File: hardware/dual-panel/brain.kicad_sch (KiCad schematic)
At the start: 75 parts, among them J1 USB_C_Receptacle_USB2.0_16P, J14 Conn_01x17, J15 Conn_01x17, SW2 BOOTSEL, U1 RP2040, U2 THVD1429, U3 W25Q32JV, U4 SN74AHCT125, U5 AMS1117-5.0, U6 AP7361C-33ER-13, U7 USBLC6-2SC6, U8 LM66200, X1 12MHz ABM8-272-T3

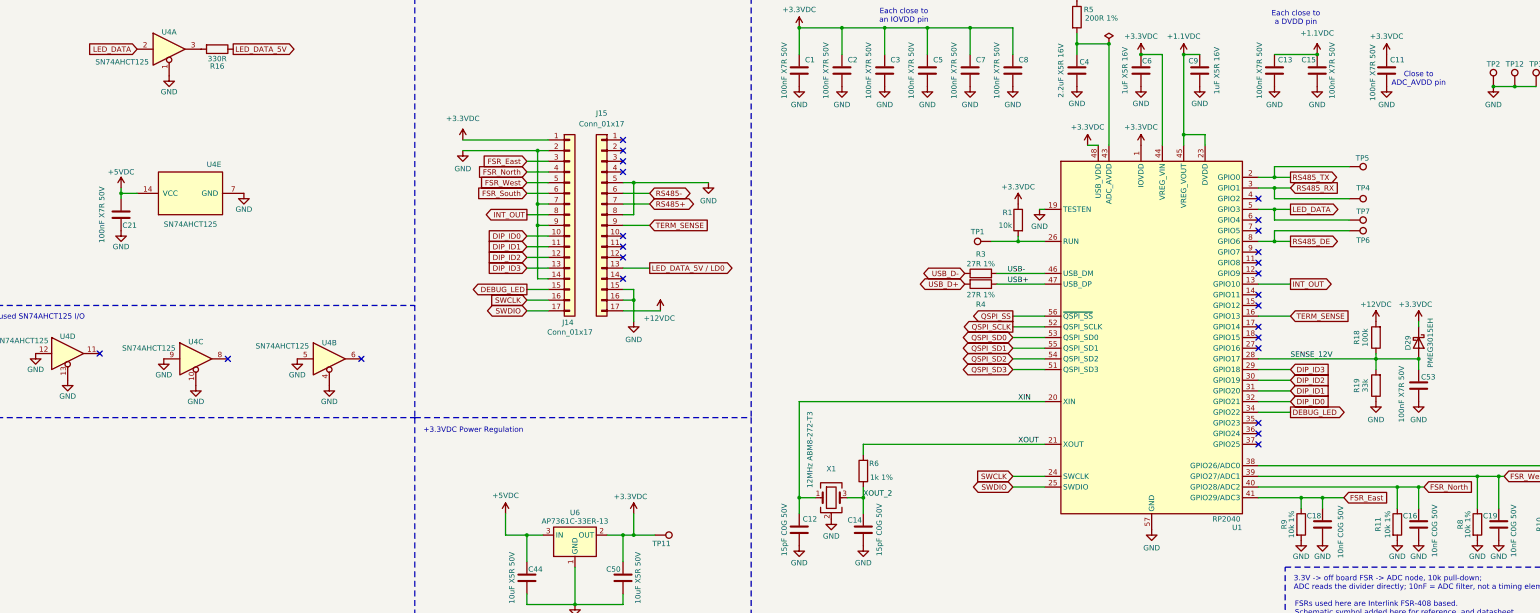
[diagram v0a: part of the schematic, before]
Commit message: dual-panel: brain laid out, interface reworked to 4x 1x8, carrier routed
Work in progress checkpoint — not clean yet, see below.

Interface replaced: the two 1x17 rows became four 1x8 connectors, placed
in the two continuous free bands across the carrier (y~49-58 and y~83-92).
Carrier headers J12/J13/J14/J15 mate with brain sockets J2/J19/J17/J18;
both boards use the same relative layout, since the brain is translated
under the carrier rather than flipped. Grouped by function so the FSR
lines and the fast signals land on separate connectors.

Brain outline drawn at 76.1 x 63.6mm with its own GND_Brain pour, sitting
inside the measured 88 x 100mm frame opening with ~6mm per side in X.
Two M3 holes added per board (carrier H5/H6, brain H1/H2), registered to
the connectors; screw enters from the brain underside with a nut above
the carrier.

Cavity measured: 6mm from the carrier underside to the frame floor, plus
14mm to the cavity bottom, so 20mm of depth inside the opening. That
retires the depth gate and also means the carrier's four remaining
bottom-side parts (D30, R17, R20, C57, tallest 2.3mm) can stay put.

Known open, to fix next:
- +3.3VDC may be split into three islands with the regulator in only one
- +12VDC and VBUS each broken on the brain; VBUS leaves U8 unfed
- FSR_West does not land on R8 pad 1; J1 shell pad floating
- QSPI_SCLK clears GND_Brain by 0 in four places
- 180-degree rotation is only blocked by 0.50mm at the connectors; wants
  a 2.54mm Y delta between J15 and J14 for a half-pitch refusal
- screw scheme needs a board-to-board spacer, and the nuts land inside
  the LED field
- silkscreen deliberately untouched (110 of 115 DRC violations)

ERC 0, schematic parity 0. 25 unconnected, of which roughly 19 are the
expected cross-gap airwires at the mating connectors.
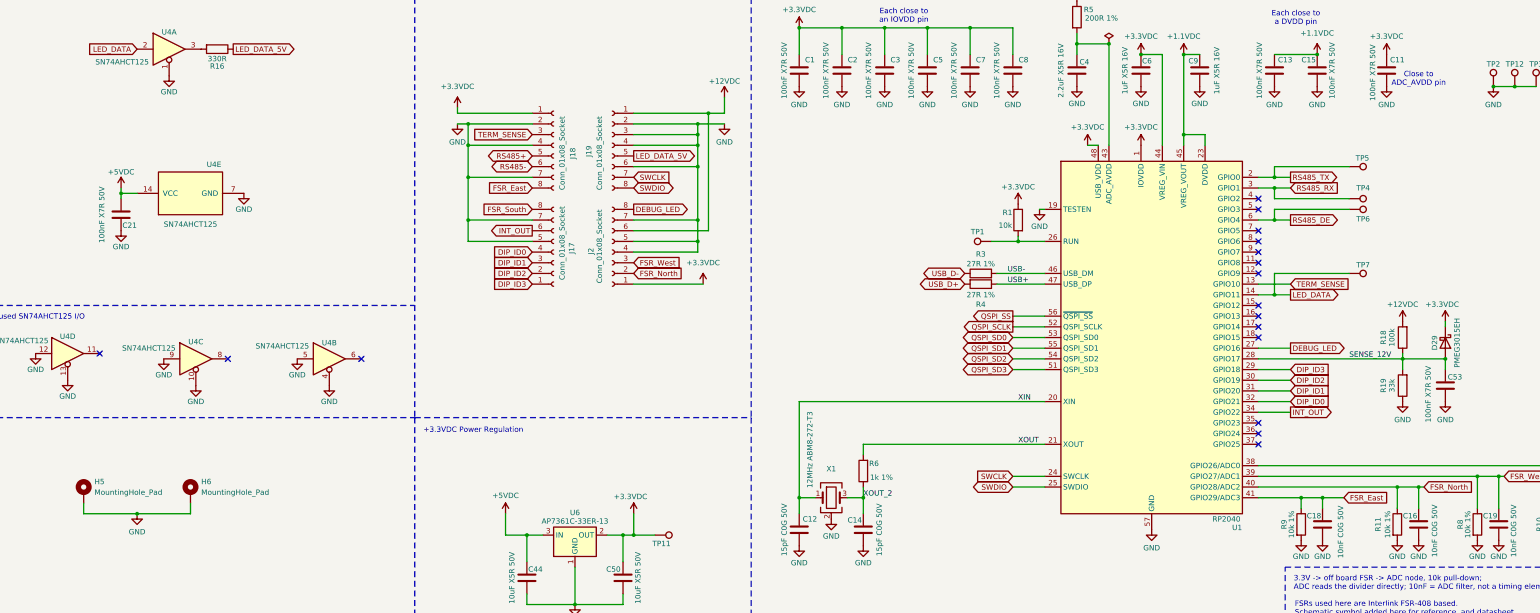
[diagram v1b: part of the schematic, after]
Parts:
- removed J14, J15: Conn_01x17, Connector_PinHeader_2.54mm:PinHeader_1x17_P2.54mm_Vertical, symbol Connector_Generic:Conn_01x17
- added H5, H6: MountingHole_Pad, MountingHole:MountingHole_3.2mm_M3_Pad, symbol Mechanical:MountingHole_Pad
- added J17, J18, J19, J2: Conn_01x08_Socket, Connector_PinSocket_2.54mm:PinSocket_1x08_P2.54mm_Vertical, symbol Connector:Conn_01x08_Socket
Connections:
- net +12VDC: now also J19.1 (Pin_1), J2.6 (Pin_6)
- net +3.3VDC: now also J18.1 (Pin_1), J2.1 (Pin_1)
- net DEBUG_LED: now also U1.27 (GPIO16), J2.8 (Pin_8); no longer U1.34 (GPIO22)
- net DIP_ID0: now also J17.4 (Pin_4)
- net DIP_ID1: now also J17.3 (Pin_3)
- net DIP_ID2: now also J17.2 (Pin_2)
- net DIP_ID3: now also J17.1 (Pin_1)
- net FSR_East: now also J18.8 (Pin_8)
- net FSR_North: now also J2.2 (Pin_2)
- net FSR_South: now also J17.8 (Pin_8)
- net FSR_West: now also J2.3 (Pin_3)
- net GND: now also H5.1, H6.1, J17.5 (Pin_5), J17.7 (Pin_7), J18.2 (Pin_2), J18.4 (Pin_4), J18.7 (Pin_7), J19.2 (Pin_2), J19.3 (Pin_3), J19.4 (Pin_4), J19.6 (Pin_6), J2.4 (Pin_4), J2.5 (Pin_5), J2.7 (Pin_7)
- net INT_OUT: now also U1.34 (GPIO22), J17.6 (Pin_6); no longer U1.13 (GPIO10)
- net LED_DATA: now also U1.14 (GPIO11); no longer U1.5 (GPIO3)
- net LED_DATA_5V: now also J19.5 (Pin_5)
- net RS485+: now also J18.5 (Pin_5)
- net RS485-: now also J18.6 (Pin_6)
- net RS485_DE: now also U1.6 (GPIO4); no longer U1.8 (GPIO6)
- net SWCLK: now also J19.7 (Pin_7)
- net SWDIO: now also J19.8 (Pin_8)
- net TERM_SENSE: now also U1.13 (GPIO10), J18.3 (Pin_3); no longer U1.16 (GPIO13)
- no-connect marks 30 -> 22
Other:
- moved on the sheet: C53, D29, R18, R19, TP6, TP7

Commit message: R8-R11: switch 10k 1% to C98220 for JLC stock
C5713432 was short at JLC, so the FSR divider legs move to C98220. Applied to
both designs, schematic and PCB, since dual-panel and panel-pcb share the part.
C5713432 was used only by these four, so the swap is unambiguous.

These are the FSR voltage-divider legs on the brain, paired with C16-C19. The
mapping is not sequential: N->R11/C16, E->R9/C18, S->R10/C17, W->R8/C19.
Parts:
- R10, R11, R8, R9: LCSC C5713432 -> C98220
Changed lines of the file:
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@@
 			)
 		)
-		(property "LCSC" "C5713432"
+		(property "LCSC" "C98220"
 			(at 386.08 144.78 0)
 			(hide yes)
@@
 			)
 		)
-		(property "LCSC" "C5713432"
+		(property "LCSC" "C98220"
 			(at 347.98 144.78 0)
 			(hide yes)
@@
 			)
 		)
-		(property "LCSC" "C5713432"
+		(property "LCSC" "C98220"
 			(at 325.12 144.78 0)
 			(hide yes)
@@
 			)
 		)
-		(property "LCSC" "C5713432"
+		(property "LCSC" "C98220"
 			(at 367.03 144.78 0)
 			(hide yes)

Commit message: dual-panel: per-sheet refdes blocks, stitching vias, silkscreen
Reference designators are now numbered in per-sheet blocks — carrier 2xx,
brain 3xx — so a designator says which of the two boards a part sits on.
That is the multi-sheet exception the review conventions allow, and it is
cheaper than closing every gap left by seeding both sheets from panel-pcb
and stripping them down. No designator is duplicated across the sheets.

Also: ground stitching vias (464 -> 1071), the year appended to both
name/rev blocks, and the fab order-number placeholder removed.

Note for the next renumber: "Update PCB from Schematic" will refuse to
match and offer to re-add every footprint. The links are fine — it is the
sticky "re-link by reference designator" option, which cannot match once
every designator has changed. Recovery is to revert the annotation,
re-link once while the designators still agree, then reannotate. The
underlying cause is that dual-panel.kicad_pro registers the root sheet as
a1b2c3d4-...-000000000001, which is panel-pcb's root UUID, while
dual-panel.kicad_sch says ...00000000d001.

DRC 0, ERC 0 with zones refilled. 19 unconnected and 93 net_conflict
remain, unchanged from before this commit: the 19 are the board-to-board
mating gap KiCad cannot model, the 93 are pre-existing net-name
disagreements on the WS2815 VCC/PWR_FLAG nets.
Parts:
- renumbered C21 to C301, C52 to C302, C44 to C303, C54 to C304, C56 to C305, C37 to C306, C50 to C307, C38 to C308, C55 to C309, C1 to C310, C12 to C311, C2 to C312, C14 to C313, C3 to C314, C5 to C315, C7 to C316, C8 to C317, C4 to C318, C6 to C319, C9 to C320, C13 to C321, C15 to C322, C20 to C323, C18 to C324, C11 to C325, C16 to C326, C53 to C327, C10 to C328, C19 to C329, C17 to C330, D12 to D301, D23 to D302, D29 to D303, FSR1 to FSR301, H5 to H301, H6 to H302, J18 to J301, J17 to J302, J19 to J303, J2 to J304, J1 to J305, R16 to R301, R6 to R302, R13 to R303, R14 to R304, R3 to R305, R4 to R306, R1 to R307, R5 to R308, R7 to R309, R12 to R310, R9 to R311, R11 to R312, R18 to R313, R19 to R314, R8 to R315, R10 to R316, SW2 to SW301, TP11 to TP301, TP10 to TP302, TP1 to TP303, TP5 to TP304, TP4 to TP305, TP6 to TP306, TP7 to TP307, TP2 to TP308, TP12 to TP309, TP3 to TP310, TP13 to TP311, TP14 to TP312, U4 to U301, U6 to U302, U5 to U303, U8 to U304, U7 to U305, U1 to U306, U3 to U307, U2 to U308, X1 to X301

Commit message: shifter: swap quad SN74AHCT125 for single-gate SN74AHCT1G125 on all boards
External review suggested 74LVC1G34/74LVC1G17 since only one gate was used;
LVC was rejected on input thresholds (VIH = 0.7*VCC = 3.5V at 5V; the 1G17's
Schmitt VT+ max hits 3.33V at 5.5V) but the single-gate idea was right.
SN74AHCT1G125DBVR keeps AHCT's guaranteed TTL VIH of 2.0V in a SOT-23-5:
LCSC C7484, DigiKey 296-4708-1-ND. OE tied to GND; decoupling caps kept.

- panel-pcb U4, dual-panel brain U301, master-pcb U3: schematic symbol,
  footprint, placement and routing redone; spare-gate GND ties and
  no-connects removed
- panel: +5V feed re-routed with a short B.Cu hop under the LED_DATA riser
- master: DIP-14 replaced by SMD; new via drops the B.Cu underglow trace
  onto the A pad, new GND via feeds the OE pad's thermal spokes
- docs + BOMs updated (CLAUDE.md, PANEL_PCB, MASTER_PCB, BOM, UNDERGLOW,
  PRE_ORDER_CHECKLIST, dual-panel README, master-pcb-BOM.csv)

Verification: ERC 0 on all three projects; DRC 0 on panel and master;
dual-panel at its expected floor (19 cross-gap airwires, 90 pre-existing
PWR_FLAG parity conflicts, down from 92).
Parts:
- removed U301: SN74AHCT125, Package_SO:SOIC-14_3.9x8.7mm_P1.27mm, symbol 74xx:74AHCT125
- added U301: SN74AHCT1G125, Package_TO_SOT_SMD:SOT-23-5, symbol 74xGxx:74AHCT1G125
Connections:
- net +5VDC: now also U301.5 (VCC)
- net GND: now also U301.1, U301.3 (GND)
- net LED_DATA: now also U301.2
- net at R301.2: now also U301.4
- no-connect marks 22 -> 19
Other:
- note removed: "Unused SN74AHCT125 I/O"
- moved on the sheet: C301, R301, TP309, TP310

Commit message: dual-panel: third mounting hole, fix hole refdes, set via fill/cap
Adds a third M3 fixing to both boards and moves the top one, which removes
the rocking degree of freedom the two-screw mount still had. With only two
screws the boards could rotate about the axis through them, and the two
board-to-board sockets furthest off that axis sat 27mm and 34mm out. Three
non-collinear fixings constrain the plane outright.

  arrangement                 worst socket-to-screw   support triangle
  2 screws (before)                   45.99 mm        none (collinear)
  old top + new bottom-right          41.46 mm        1576 mm2
  top moved + new bottom-right        32.07 mm        1583 mm2

Brain/carrier hole pairs stay on the exact (101.68, -16.87) offset.

Mounting hole refdes were swapped against the 2xx=carrier / 3xx=brain
convention: H201/H202 sat on the brain and H301/H302 on the carrier. The
schematic sheets were already right, so this swaps the footprint placements
only, leaving the symbol-to-footprint paths untouched. Their reference-text
offsets were swapped too, since those were tuned per location (a -0.81mm
nudge to clear J302's label, and one text placed below to stay off the
brain's top edge) and would otherwise have collided in their new homes.

Sets board-level via capping and filling ahead of ordering with JLC's epoxy
fill option. This is annotation only -- verified it changes nothing in the
Gerbers, drill, gerber job file, IPC-2581 or ODB++ output. Set at board level
rather than per-via because every via reads FROM_BOARD, and because the fill
is a whole-board process, not a per-via selection.

Also restores via tenting, which had been switched off. That opened a solder
mask window over all 1107 vias -- a bridging risk in assembly, and the cause
of 138 silkscreen-clipped-by-mask violations.

Stitching vias re-added after the clearance rework: 1107 total (1014 GND).
Carrier stitching matches the pre-rework board exactly (790 GND vias, median
GND-pad-to-via 1.55mm,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
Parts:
- added H303: MountingHole_Pad, MountingHole:MountingHole_3.2mm_M3_Pad, symbol Mechanical:MountingHole_Pad
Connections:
- net GND: now also H303.1
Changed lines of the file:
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@@
 	)
 	(junction
-		(at 48.26 142.24)
-		(diameter 0)
-		(color 0 0 0 0)
-	)
-	(junction
 		(at 127 54.61)
 		(diameter 0)
@@
 	)
 	(junction
+		(at 60.96 142.24)
+		(diameter 0)
+		(color 0 0 0 0)
+	)
+	(junction
 		(at 142.24 198.12)
 		(diameter 0)
@@
 	(wire
 		(pts
+			(xy 86.36 139.7) (xy 86.36 142.24)
+		)
+		(stroke
+			(width 0)
+			(type default)
+		)
+	)
+	(wire
+		(pts
+			(xy 86.36 142.24) (xy 60.96 142.24)
+		)
+		(stroke
+			(width 0)
+			(type default)
+		)
+	)
+	(wire
+		(pts
 			(xy 158.75 259.08) (xy 158.75 273.05)
 		)
@@
 	(wire
 		(pts
-			(xy 48.26 142.24) (xy 35.56 142.24)
+			(xy 35.56 142.24) (xy 60.96 142.24)
 		)
 		(stroke
@@
 	(wire
 		(pts
-			(xy 48.26 142.24) (xy 60.96 142.24)
-		)
-		(stroke
-			(width 0)
-			(type default)
-		)
-	)
-	(wire
-		(pts
 			(xy 228.6 203.2) (xy 231.14 203.2)
 		)
@@
 	)
 	(symbol
+		(lib_id "Mechanical:MountingHole_Pad")
+		(at 86.36 137.16 0)
+		(unit 1)
+		(body_style 1)
+		(exclude_from_sim no)
+		(in_bom no)
+		(on_board yes)
+		(in_pos_files yes)
+		(dnp no)
+		(fields_autoplaced yes)
+		(property "Reference" "H303"
+			(at 88.9 134.6199 0)
+			(show_name no)
+			(do_not_autoplace no)
+			(effects
+				(font
+					(size 1.27 1.27)
+				)
+				(justify left)
+			)
+		)
+		(property "Value" "MountingHole_Pad"
+			(at 88.9 137.1599 0)
+			(show_name no)
+			(do_not_autoplace no)
+			(effects
+				(font
+					(size 1.27 1.27)
+				)
+				(justify left)
+			)
+		)
+		(property "Footprint" "MountingHole:MountingHole_3.2mm_M3_Pad"
+			(at 86.36 137.16 0)
+			(hide yes)
+			(show_name no)
+			(do_not_autoplace no)
+			(effects
+				(font
+					(size 1.27 1.27)
+				)
+			)
+		)
+		(property "Datasheet" ""
+			(at 86.36 137.16 0)
+			(hide yes)
+			(show_name no)
+			(do_not_autoplace no)
+			(effects
+				(font
+					(size 1.27 1.27)
+				)
+			)
+		)
+		(property "Description" "Mounting Hole with connection"
+			(at 86.36 137.16 0)
+			(hide yes)
+			(show_name no)
+			(do_not_autoplace no)
+			(effects
+				(font
+					(size 1.27 1.27)
+				)
+			)
+		)
+		(pin "1"
+		)
+		(instances
+			(project "dual-panel"
+				(path "/a1b2c3d4-0000-4000-8000-000000000001/a1b2c3d4-0000-4000-8000-00000000db01"
+					(reference "H303")
+					(unit 1)
+				)
+			)
+		)
+	)
+	(symbol
 		(lib_id "Connector:TestPoint")
 		(at 378.46 40.64 0)
@@
 	(symbol
 		(lib_id "power:GND")
-		(at 48.26 142.24 0)
+		(at 60.96 142.24 0)
 		(unit 1)
 		(body_style 1)
@@
 		(dnp no)
 		(property "Reference" "#PWR0305"
-			(at 48.26 147.32 0)
+			(at 60.96 147.32 0)
 			(hide yes)
 			(show_name no)
@@
 		)
 		(property "Value" "GND"
-			(at 48.26 146.558 0)
+			(at 60.96 146.558 0)
 			(show_name no)
 			(do_not_autoplace no)
@@
 		)
 		(property "Footprint" ""
-			(at 48.26 142.24 0)
+			(at 60.96 142.24 0)
 			(hide yes)
 			(show_name no)
@@
 		)
 		(property "Datasheet" ""
-			(at 48.26 142.24 0)
+			(at 60.96 142.24 0)
 			(hide yes)
 			(show_name no)
@@
 		)
 		(property "Description" "Power symbol creates a global label with name \"GND\" , ground"
-			(at 48.26 142.24 0)
+			(at 60.96 142.24 0)
 			(hide yes)
 			(show_name no)

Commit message: rev1: order both boards, and freeze exactly what went to fab
Boards are at JLCPCB as of 2026-08-18. Everything after this commit is rev 2.

Four design changes made on order day, all verified before submitting:

- U306 RP2040 signal pads 0.20 -> 0.23 mm, matching Raspberry Pi's official
  land pattern, via a local footprint. Length/pitch/centres/EP unchanged.
  Needed a zone refill and scoping the QSPI pour rule to B.Type == 'Zone'
  (it had no B-side condition, so it was policing track-to-pad too).
- RS-485 transceiver THVD1429 -> THVD1450DR on BOTH boards. Identical SOIC-8
  pinout. Gives up on-die IEC 61000-4-5 surge, which TI scopes to lightning and
  power-grid transients; gains 18 kV vs 8 kV contact ESD, the threat this pad
  actually documents. Also -$52 and 84x the stock, retiring the BOM's tightest
  line (60 units).
- 10 nF ADC filter caps C57112 -> C723749. The old part was X7R while the
  schematic said C0G; these are the four FSR ADC inputs, where Class II's
  piezoelectric response would inject charge synchronously with a footstep.
  Found by auditing all 35 BOM lines against live LCSC pages.
- master-pcb: 297 vias 0.45 -> 0.60 mm (0.075 -> 0.150 mm annular), after
  running DFM on the master for the first time. A quote is not a DFM check.

Both boards re-verified after every change: dual-panel 0/19/90/0,
master 0/0/0/0.

Adds hardware/fab-archive/rev1-2026-08-18/ with the byte-exact artifacts that
were manufactured, plus SHA256SUMS and a .gitattributes that disables CRLF
normalisation so they stay byte-exact. hardware/**/production/ is gitignored,
so without this there would be no record in git of what was physically built.

Adds QUOTE-2026-08-18.md (the real qty-20 quote; the July one is now marked
superseded) and splits the JLC order notes into PCB and PCBA remark blocks,
each within the 500-character limit the order form imposes.
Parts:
- C304, C305, C319, C320: value 1uF X5R 16V -> 1uF X5R 25V
- C324, C326, C329, C330: value 10nF C0G 50V -> 10nF C0G 25V; LCSC C57112 -> C723749
- R305, R306: LCSC C858950 -> C25190
- U306: footprint Package_DFN_QFN:QFN-56-1EP_7x7mm_P0.4mm_EP3.2x3.2mm -> dual-panel:QFN-56-1EP_7x7mm_P0.4mm_EP3.2x3.2mm_RPiPad
- U308: value THVD1429 -> THVD1450; LCSC C1850236 -> C2671361; MPN THVD1429DR -> THVD1450DR
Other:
- note added: "No external bus biasing: THVD1450 has integrated open/short/idle failsafe."
- note removed: "No external bus biasing: THVD1429 has integrated open/short/idle failsafe."
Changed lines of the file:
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@@
 		)
 	)
-	(text "No external bus biasing: THVD1429 has\nintegrated open/short/idle failsafe."
+	(text "No external bus biasing: THVD1450 has\nintegrated open/short/idle failsafe."
 		(exclude_from_sim no)
 		(at 350.012 182.88 0)
@@
 			)
 		)
-		(property "Value" "10nF C0G 50V"
+		(property "Value" "10nF C0G 25V"
 			(at 375.666 146.304 90)
 			(show_name no)
@@
 			)
 		)
-		(property "LCSC" "C57112"
+		(property "LCSC" "C723749"
 			(at 372.11 144.78 0)
 			(hide yes)
@@
 			)
 		)
-		(property "Value" "1uF X5R 16V"
+		(property "Value" "1uF X5R 25V"
 			(at 141.478 227.076 90)
 			(show_name no)
@@
 			)
 		)
-		(property "Footprint" "Package_DFN_QFN:QFN-56-1EP_7x7mm_P0.4mm_EP3.2x3.2mm"
+		(property "Footprint" "dual-panel:QFN-56-1EP_7x7mm_P0.4mm_EP3.2x3.2mm_RPiPad"
 			(at 289.56 100.33 0)
 			(hide yes)
@@
 			)
 		)
-		(property "Value" "10nF C0G 50V"
+		(property "Value" "10nF C0G 25V"
 			(at 394.97 146.304 90)
 			(show_name no)
@@
 			)
 		)
-		(property "LCSC" "C57112"
+		(property "LCSC" "C723749"
 			(at 391.16 144.78 0)
 			(hide yes)
@@
 			)
 		)
-		(property "LCSC" "C858950"
+		(property "LCSC" "C25190"
 			(at 248.92 85.09 0)
 			(hide yes)
@@
 			)
 		)
-		(property "Value" "10nF C0G 50V"
+		(property "Value" "10nF C0G 25V"
 			(at 356.87 146.304 90)
 			(show_name no)
@@
 			)
 		)
-		(property "LCSC" "C57112"
+		(property "LCSC" "C723749"
 			(at 353.06 144.78 0)
 			(hide yes)
@@
 			)
 		)
-		(property "Value" "10nF C0G 50V"
+		(property "Value" "10nF C0G 25V"
 			(at 334.518 146.558 90)
 			(show_name no)
@@
 			)
 		)
-		(property "LCSC" "C57112"
+		(property "LCSC" "C723749"
 			(at 330.2 144.78 0)
 			(hide yes)
@@
 			)
 		)
-		(property "Value" "1uF X5R 16V"
+		(property "Value" "1uF X5R 25V"
 			(at 283.21 36.83 90)
 			(show_name no)
@@
 			)
 		)
-		(property "LCSC" "C858950"
+		(property "LCSC" "C25190"
 			(at 248.92 87.63 0)
 			(hide yes)
@@
 			)
 		)
-		(property "Value" "1uF X5R 16V"
+		(property "Value" "1uF X5R 25V"
 			(at 305.054 36.83 90)
 			(show_name no)
@@
 			)
 		)
-		(property "Value" "THVD1429"
+		(property "Value" "THVD1450"
 			(at 381.508 214.63 0)
 			(show_name no)
@@
 			)
 		)
-		(property "Datasheet" "https://www.ti.com/lit/ds/symlink/thvd1429.pdf"
+		(property "Datasheet" "https://www.ti.com/lit/ds/symlink/thvd1450.pdf"
 			(at 375.92 228.6 0)
 			(hide yes)
@@
 			)
 		)
-		(property "Description" "Half duplex RS-485/RS-422, 12 Mbps, 3V - 5.5V supply, ±12kV electro-static discharge (ESD) protection, with receiver/driver enable, 32 receiver drive capacity, SOIC-8"
+		(property "Description" "Half duplex RS-485, 50 Mbps, 3V-5.5V supply, +/-18kV IEC 61000-4-2 contact ESD, open/short/idle failsafe, SOIC-8"
 			(at 375.92 228.6 0)
 			(hide yes)
@@
 			)
 		)
-		(property "LCSC" "C1850236"
+		(property "LCSC" "C2671361"
 			(at 375.92 228.6 0)
 			(hide yes)
@@
 			)
 		)
-		(property "MPN" "THVD1429DR"
+		(property "MPN" "THVD1450DR"
 			(at 375.92 228.6 0)
 			(hide yes)
@@
 			)
 		)
-		(property "Value" "1uF X5R 16V"
+		(property "Value" "1uF X5R 25V"
 			(at 135.382 205.74 0)
 			(show_name no)
